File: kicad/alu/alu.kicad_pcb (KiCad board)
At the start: 4 copper layers, 102.9 x 133.3 mm, 286 parts, among them J3 DB25_Male, J4 DB37_Male, U1 SN74ALVC00, U10 SN74ALVC00, U100 SN74ALVC00, U101 SN74ALVC00, U102 SN74ALVC00, U103 SN74ALVC00, U104 SN74ALVC00, U105 SN74ALVC00, U106 SN74ALVC00, U107 SN74ALVC00, U108 SN74ALVC00, U109 SN74ALVC00, U11 SN74ALVC00, U110 SN74ALVC00, U111 SN74ALVC00, U112 SN74ALVC00, U113 SN74ALVC00, U114 SN74ALVC00, U115 SN74ALVC00, U116 SN74ALVC00, U117 SN74ALVC00, U118 SN74ALVC00, U119 SN74ALVC00, U12 SN74ALVC00, U120 SN74ALVC00, U121 SN74ALVC00, U122 SN74ALVC00, U123 SN74ALVC00, U124 SN74ALVC00, U125 SN74ALVC00, U126 SN74ALVC00, U127 SN74ALVC00, U128 SN74ALVC00, U129 SN74ALVC00, U13 SN74ALVC00, U130 SN74ALVC00, U131 SN74ALVC00, U132 SN74ALVC00, U133 SN74ALVC00, U134 SN74ALVC00, U135 SN74ALVC00, U136 SN74ALVC00, U137 SN74ALVC00, U138 SN74ALVC00, U139 SN74ALVC00, U14 SN74ALVC00, U140 SN74ALVC00, U141 SN74ALVC00, U142 SN74ALVC00, U143 SN74ALVC00, U144 SN74ALVC00, U145 SN74ALVC00, U146 SN74ALVC00, U147 SN74ALVC00, U148 SN74ALVC00, U149 SN74ALVC00, U15 SN74ALVC00, U150 SN74ALVC00, U151 SN74ALVC00, U152 SN74ALVC00, U153 SN74ALVC00, U154 SN74ALVC00, U155 SN74ALVC00, U156 SN74ALVC00, U157 SN74ALVC00, U158 SN74ALVC00, U159 SN74ALVC00, U16 SN74ALVC00, U160 SN74ALVC00, U161 SN74ALVC00, U162 SN74ALVC00, U163 SN74ALVC00, U164 SN74ALVC00, U165 SN74ALVC00, U166 SN74ALVC00, U17 SN74ALVC00, U18 SN74ALVC00, U19 SN74ALVC00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

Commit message: ALU schematic, layout, routing complete. Associated motherboardmod. Also added Load LED to register and program counter boards.
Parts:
- added C5: 100uF, Capacitor_THT:CP_Radial_D8.0mm_P2.50mm, F.Cu at (236.2, 88.9)
- added C6: 100nF, Capacitor_THT:C_Disc_D5.0mm_W2.5mm_P5.00mm, F.Cu at (234.9, 82.5)
- added Q1: Q_NPN_Darlington_BEC, Package_TO_SOT_SMD:SOT-23, F.Cu at (215.3, 45.7)
- added Q2: Q_NPN_Darlington_BEC, Package_TO_SOT_SMD:SOT-23, F.Cu at (234.3, 148.0)
- added R58: 5k, Resistor_SMD:R_1206_3216Metric, F.Cu at (220.3, 48.3)
- added R59: 5k, Resistor_SMD:R_1206_3216Metric, F.Cu at (238.8, 148.0)
- moved U101 262.8 mm to (214.6, 102.2)
- moved U105 262.5 mm to (224.8, 94.6)
- moved U99 261.2 mm to (214.6, 87.0)
- moved U100 255.4 mm to (214.6, 94.6)
- moved U111 250.1 mm to (224.8, 109.9)
- moved U102 249.9 mm to (224.8, 102.2)
- moved U106 249.0 mm to (214.6, 109.9)
- moved U113 247.5 mm to (214.6, 117.5)
- moved U108 246.4 mm to (194.3, 102.2)
- moved U107 244.0 mm to (204.5, 94.6)
- moved U109 242.8 mm to (204.5, 102.2)
- moved D1 241.7 mm to (205.7, 34.3), turned to 270 degrees
- moved U104 240.2 mm to (194.3, 94.6)
- moved U114 231.0 mm to (204.5, 117.5)
- moved U110 227.6 mm to (194.3, 109.9)
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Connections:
- J3 pad 5: Net-(J3-Pad5) -> inst_15
- R1 pad 1: GND -> /LEDs/coll
- R10 pad 1: GND -> /LEDs/coll
- R11 pad 1: GND -> /LEDs/coll
- R12 pad 1: GND -> /LEDs/coll
- R13 pad 1: GND -> /LEDs/coll
- R14 pad 1: GND -> /LEDs/coll
- R15 pad 1: GND -> /LEDs/coll
- R16 pad 1: GND -> /LEDs/coll
- R17 pad 1: GND -> /LEDs/coll
- R18 pad 1: GND -> /LEDs/coll
- R19 pad 1: GND -> /LEDs/coll
- R2 pad 1: GND -> /LEDs/coll
- R20 pad 1: GND -> /LEDs/coll
- R21 pad 1: GND -> /LEDs/coll
- R22 pad 1: GND -> /LEDs/coll
- R23 pad 1: GND -> /LEDs/coll
- R24 pad 1: GND -> /LEDs/coll
- R25 pad 1: GND -> /LEDs/coll
- R26 pad 1: GND -> /LEDs/coll
- R27 pad 1: GND -> /LEDs/coll
- R28 pad 1: GND -> /LEDs/coll
- R29 pad 1: GND -> /LEDs/coll
- R3 pad 1: GND -> /LEDs/coll
- R30 pad 1: GND -> /LEDs/coll
- R31 pad 1: GND -> /LEDs/coll
- R32 pad 1: GND -> /LEDs/coll
- R33 pad 1: GND -> /LEDs/coll
- R34 pad 1: GND -> /LEDs/coll
- R35 pad 1: GND -> /LEDs/coll
- R36 pad 1: GND -> /LEDs/coll
- R37 pad 1: GND -> /LEDs/coll2
- R38 pad 1: GND -> /LEDs/coll2
- R39 pad 1: GND -> /LEDs/coll2
- R4 pad 1: GND -> /LEDs/coll
- R40 pad 1: GND -> /LEDs/coll2
- R41 pad 1: GND -> /LEDs/coll2
- R42 pad 1: GND -> /LEDs/coll2
- R43 pad 1: GND -> /LEDs/coll2
- R44 pad 1: GND -> /LEDs/coll2
- R45 pad 1: GND -> /LEDs/coll2
- R46 pad 1: GND -> /LEDs/coll2
- R47 pad 1: GND -> /LEDs/coll2
- R48 pad 1: GND -> /LEDs/coll2
- R49 pad 1: GND -> /LEDs/coll2
- R5 pad 1: GND -> /LEDs/coll
- R50 pad 1: GND -> /LEDs/coll2
- R51 pad 1: GND -> /LEDs/coll2
- R52 pad 1: GND -> /LEDs/coll2
- R53 pad 1: GND -> /LEDs/coll2
- R54 pad 1: GND -> /LEDs/coll2
- R55 pad 1: GND -> /LEDs/coll2
- R56 pad 1: GND -> /LEDs/coll2
- R57 pad 1: GND -> /LEDs/coll2
- R6 pad 1: GND -> /LEDs/coll
- R7 pad 1: GND -> /LEDs/coll
- R8 pad 1: GND -> /LEDs/coll
- R9 pad 1: GND -> /LEDs/coll
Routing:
- net no: track 0.00 -> 435.1 mm, vias 0 -> 26
- net /LEDs/coll: track 0.00 -> 385.6 mm
- net f: track 0.00 -> 384.3 mm, vias 0 -> 18
- net nx: track 0.00 -> 382.1 mm, vias 0 -> 19
- net ny: track 0.00 -> 378.7 mm, vias 0 -> 19
- net ~f: track 0.00 -> 356.0 mm, vias 0 -> 15
- net ~no: track 0.00 -> 322.0 mm, vias 0 -> 25
- net zy: track 0.00 -> 313.5 mm, vias 0 -> 4
- net zx: track 0.00 -> 313.1 mm, vias 0 -> 4
- net out15: track 0.00 -> 290.5 mm, vias 0 -> 3
- net ~nx: track 0.00 -> 254.6 mm, vias 0 -> 17
- net ~ny: track 0.00 -> 243.9 mm, vias 0 -> 17
- net ~zx: track 0.00 -> 236.4 mm, vias 0 -> 9
- net GND: track 0.00 -> 232.1 mm, vias 0 -> 2
- net out_zero: track 0.00 -> 231.4 mm, vias 0 -> 2
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- added copper zone on B.Cu, net +3V3
- added copper zone on F.Cu, net GND
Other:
- board size 102.9 x 133.3 mm -> 207 x 132.1 mm
- board text added: "(x & y)"
- board text added: "(x + y)"
- board text added: "is neg"
- board text added: "is zero"
- board text added: "not out"
- board text added: "not x"
- board text added: "not y"
- board text added: "out0"
- board text added: "out1"
- board text added: "out10"
- board text added: "out11"
- board text added: "out12"
- board text added: "out13"
- board text added: "out14"
- board text added: "out15"
- board text added: "out2"
- board text added: "out3"
- board text added: "out4"
- board text added: "out5"
- board text added: "out6"
- board text added: "out7"
- board text added: "out8"
- board text added: "out9"
- board text added: "x0"
- board text added: "x1"
- board text added: "x10"
- board text added: "x11"
- board text added: "x12"
- board text added: "x13"
- board text added: "x14"
- board text added: "x15"
- board text added: "x2"
- board text added: "x3"
- board text added: "x4"
- board text added: "x5"
- board text added: "x6"
- board text added: "x7"
- board text added: "x8"
- board text added: "x9"
- board text added: "y0"
- board text added: "y1"
- board text added: "y10"
- board text added: "y11"
- board text added: "y12"
- board text added: "y13"
- board text added: "y14"
- board text added: "y15"
- board text added: "y2"
- board text added: "y3"
- board text added: "y4"
- board text added: "y5"
- board text added: "y6"
- board text added: "y7"
- board text added: "y8"
- board text added: "y9"
- board text added: "zero x"
- board text added: "zero y"

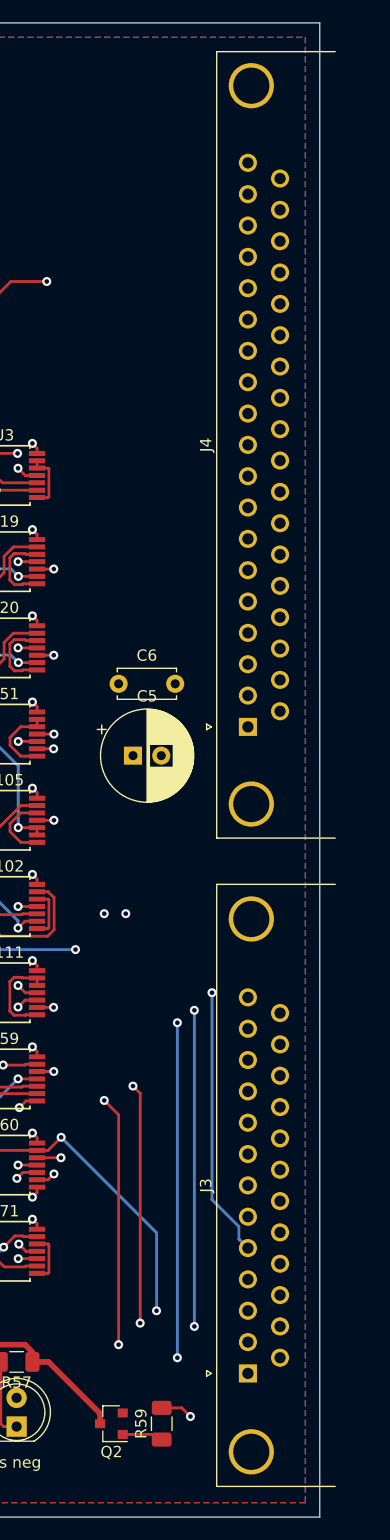
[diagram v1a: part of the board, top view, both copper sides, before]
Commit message: Readme updates (#6)
* Readme intro section

* Board revisions for manufacturing, add digikey PNs to all, added logo.
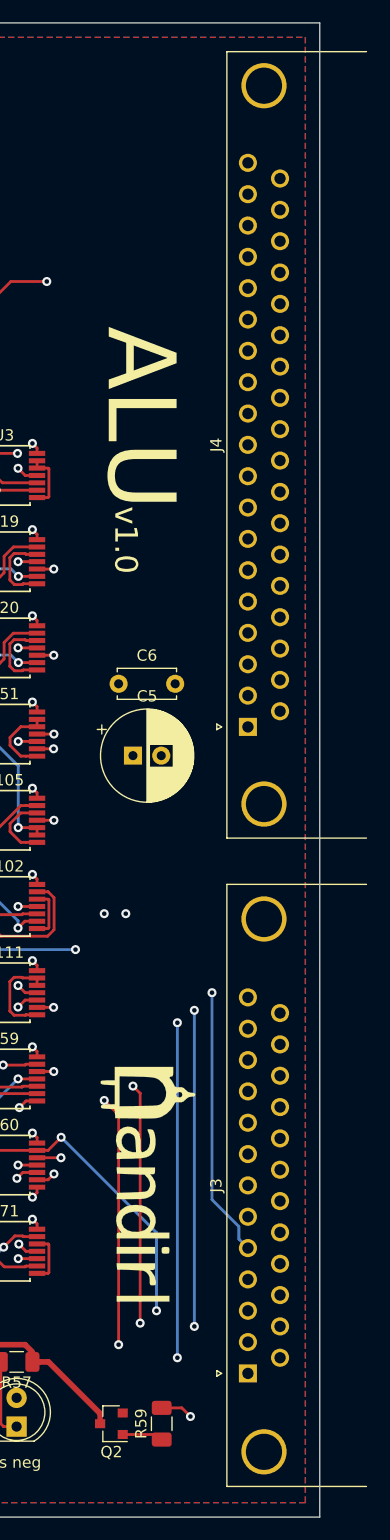
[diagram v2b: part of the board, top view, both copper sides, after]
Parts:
- added G***: LOGO, nandirl logo:logo_sm, F.Cu at (237.5, 127.0)
- J3: footprint Connector_Dsub:DSUB-25_Male_Horizontal_P2.77x2.84mm_EdgePinOffset4.94mm_Housed_MountingHolesOffset7.48mm -> Connector_Dsub:DSUB-25_Male_Horizontal_P2.77x2.84mm_EdgePinOffset7.70mm_Housed_MountingHolesOffset9.12mm
- J4: footprint Connector_Dsub:DSUB-37_Male_Horizontal_P2.77x2.84mm_EdgePinOffset4.94mm_Housed_MountingHolesOffset7.48mm -> Connector_Dsub:DSUB-37_Male_Horizontal_P2.77x2.84mm_EdgePinOffset7.70mm_Housed_MountingHolesOffset9.12mm
- R1, R10, R11, R12, R13, R14, R15, R16, R17, R18, R19, R2, R20, R21, R22, R23, R24, R25, R26, R27, R28, R29, R3, R30, R31, R32, R33, R34, R35, R36, R37, R38, R39, R4, R40, R41, R42, R43, R44, R45, R46, R47, R48, R49, R5, R50, R51, R52, R53, R54, R55, R56, R57, R6, R7, R8, R9: value R_US -> 1K
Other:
- board text added: "ALU"
- board text added: "v1.0"
